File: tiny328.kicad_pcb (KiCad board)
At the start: 2 copper layers, 35.1 x 22.4 mm, 23 parts, among them IC1 ATMEGA328P-A, U1 RFM12, U2 MCP1702T-3302E/CB, Y1 16MHz

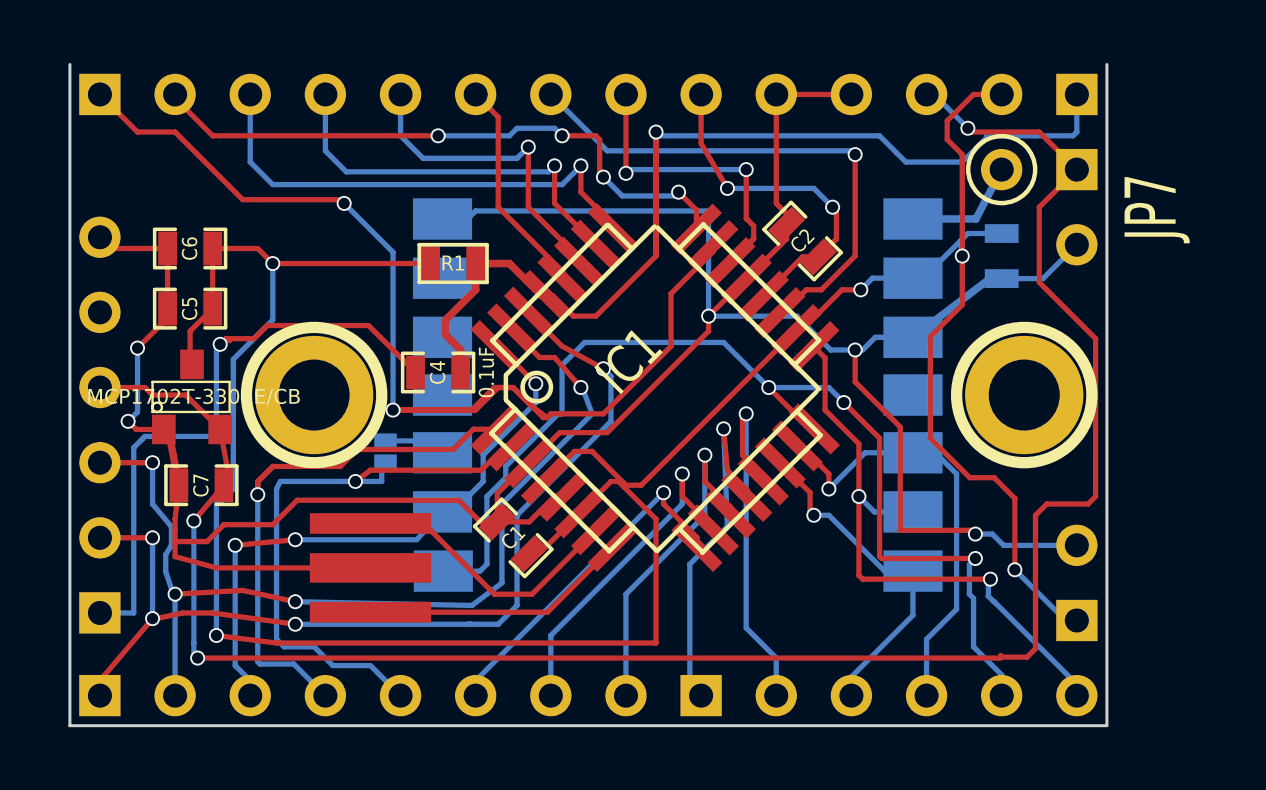
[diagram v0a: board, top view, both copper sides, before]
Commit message: increase power track widths
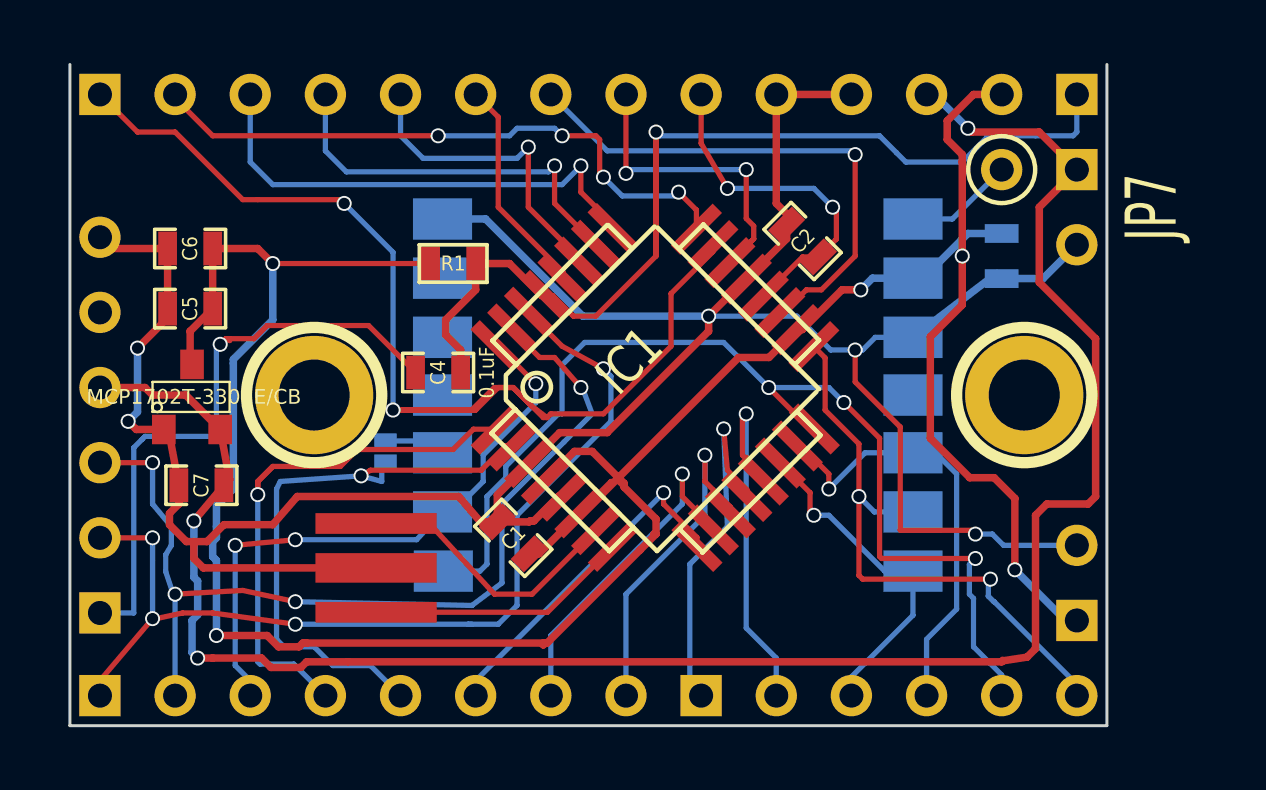
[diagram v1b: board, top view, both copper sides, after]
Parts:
- moved Y1 0.19 mm to (39.3, 31.0)
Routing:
- net GND: track 97.9 -> 95.2 mm

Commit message: widen vias
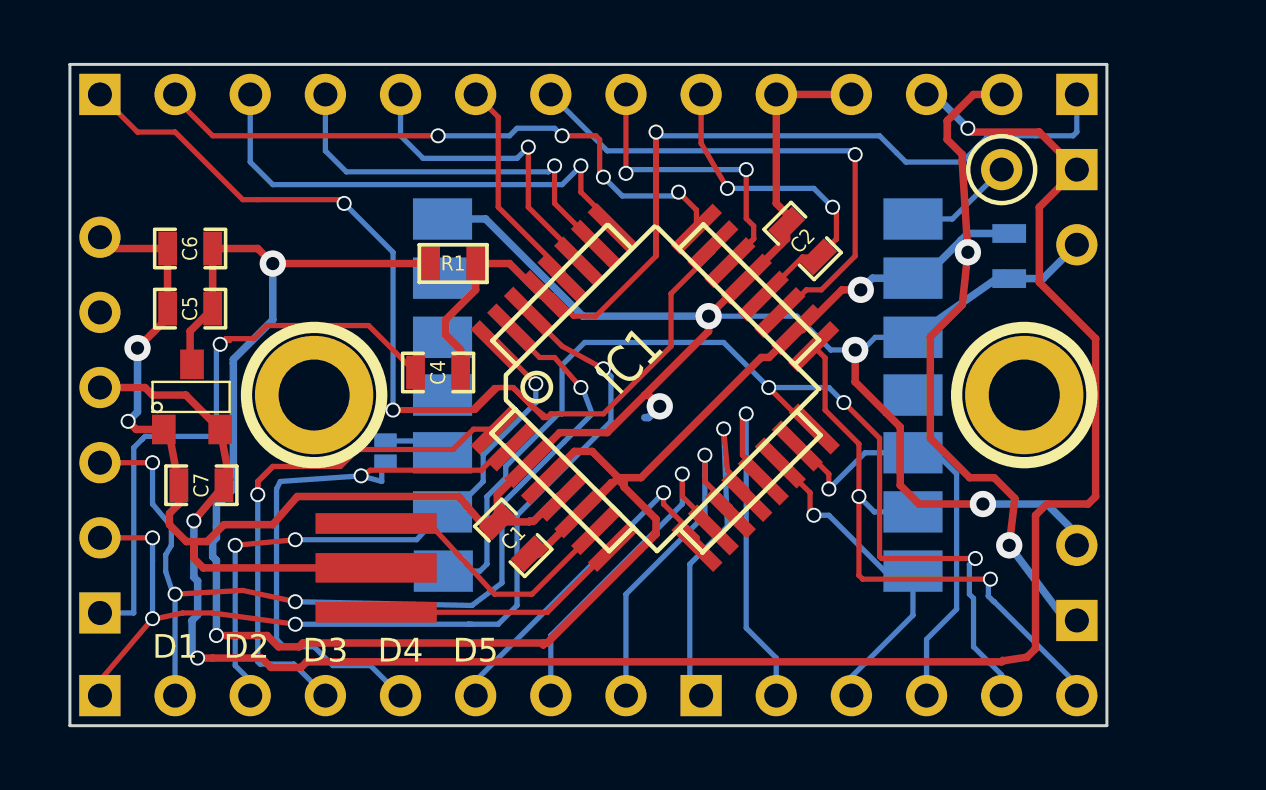
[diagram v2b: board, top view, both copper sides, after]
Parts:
- moved C3 0.25 mm to (60.7, 20.4)
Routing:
- net GND: track 95.2 -> 99.1 mm, vias 5 -> 6
- added copper zone on B.Cu, net GND
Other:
- board text added: "D1"
- board text added: "D2"
- board text added: "D3"
- board text added: "D4"
- board text added: "D5"

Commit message: all connected, flooded
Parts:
- moved C6 1.52 mm to (34.5, 20.2)
- moved C3 0.76 mm to (60.7, 21.2)
- moved C5 0.25 mm to (33.3, 22.2)
- moved C7 0.18 mm to (33.5, 28.1)
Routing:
- net GND: track 99.1 -> 102.9 mm
- net /D1/TX: track 32.8 -> 31.9 mm
- net 3V3: track 93.5 -> 94.2 mm
- net /D0/RX: track 33.1 -> 32.5 mm
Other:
- board text added: "3V3"
- board text added: "5"
- board text added: "5V"
- board text added: "6"
- board text added: "A"
- board text added: "A0"
- board text added: "A1"
- board text added: "A2"
- board text added: "A3"
- board text added: "A4"
- board text added: "A5"
- board text added: "A7"
- board text added: "ANT"
- board text added: "AREF"
- board text added: "D0 RX"
- board text added: "D1 TX"
- board text added: "D10"
- board text added: "D10*"
- board text added: "D11"
- board text added: "D11*"
- board text added: "D12"
- board text added: "D13"
- board text added: "D3*"
- board text added: "D3*I1"
- board text added: "D5*"
- board text added: "D6*"
- board text added: "D7"
- board text added: "D8"
- board text added: "D9"
- board text added: "D9*"
- board text added: "DTR"
- board text added: "GND"
- board text added: "I0"
- board text added: "I1"
- board text added: "MOSI"
- board text added: "RST"
- board text added: "RX"
- board text added: "RX D0"
- board text added: "SCL"
- board text added: "SDA"
- board text added: "SS"
- board text added: "TX"
- board text added: "TX D1"
- board text removed: "D1"
- board text removed: "D3"
- board text removed: "D5"

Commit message: all connected, flooded
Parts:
- added R2: 100K, SM0603, F.Cu at (33.4, 17.9)
- added R3: 100K, SM0603, F.Cu at (30.6, 17.8)

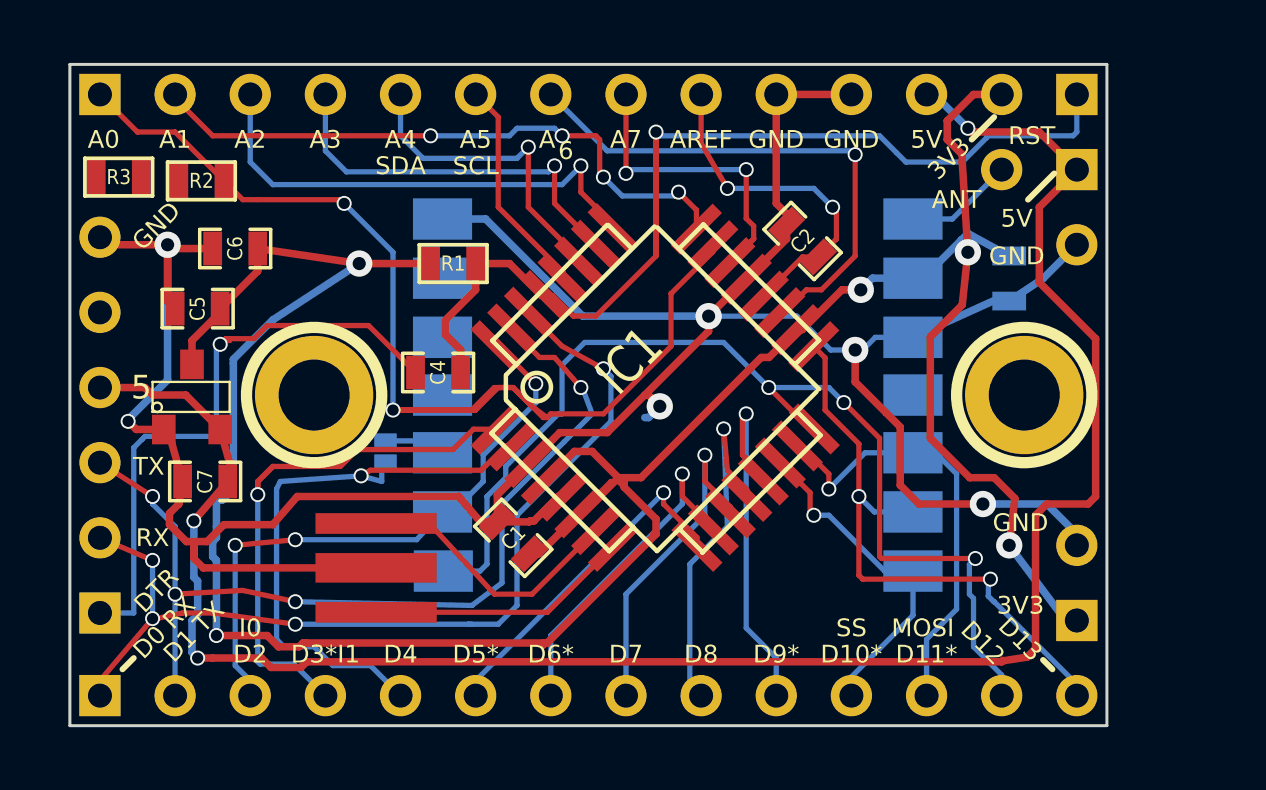
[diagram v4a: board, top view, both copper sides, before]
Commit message: first version sent to osh park
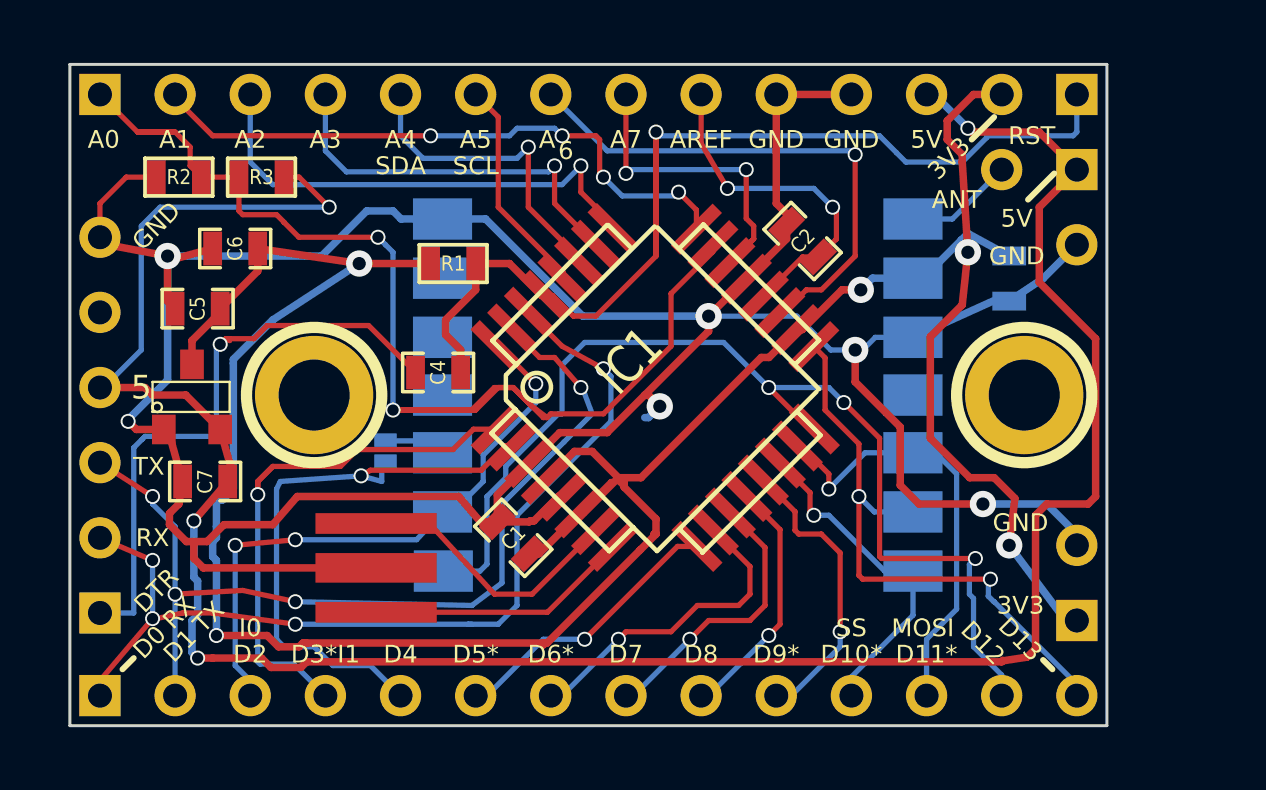
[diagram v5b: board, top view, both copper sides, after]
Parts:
- moved R3 4.83 mm to (35.4, 17.8), turned to 0 degrees
- moved R2 0.77 mm to (32.6, 17.8), turned to 180 degrees
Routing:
- net +5V: track 67.2 -> 81.9 mm, vias 3 -> 4
- net GND: track 102.9 -> 115.7 mm
- net /D8: track 12.3 -> 8.45 mm
- net /D9: track 12.5 -> 10.0 mm
- net /A0: track 42.2 -> 44.5 mm
- net /D5: track 11.8 -> 9.57 mm
- net /D7: track 11.5 -> 9.57 mm
- net /D6: track 11.7 -> 10.8 mm

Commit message: Increase header hole & pad size Fix MCP1800 reversed pins 2 & 3 Fix FTDI reversed TX & RX Add MISO & SCK labels Remove silk screen around mounting holes Increase pad size for 0603's for hand soldering
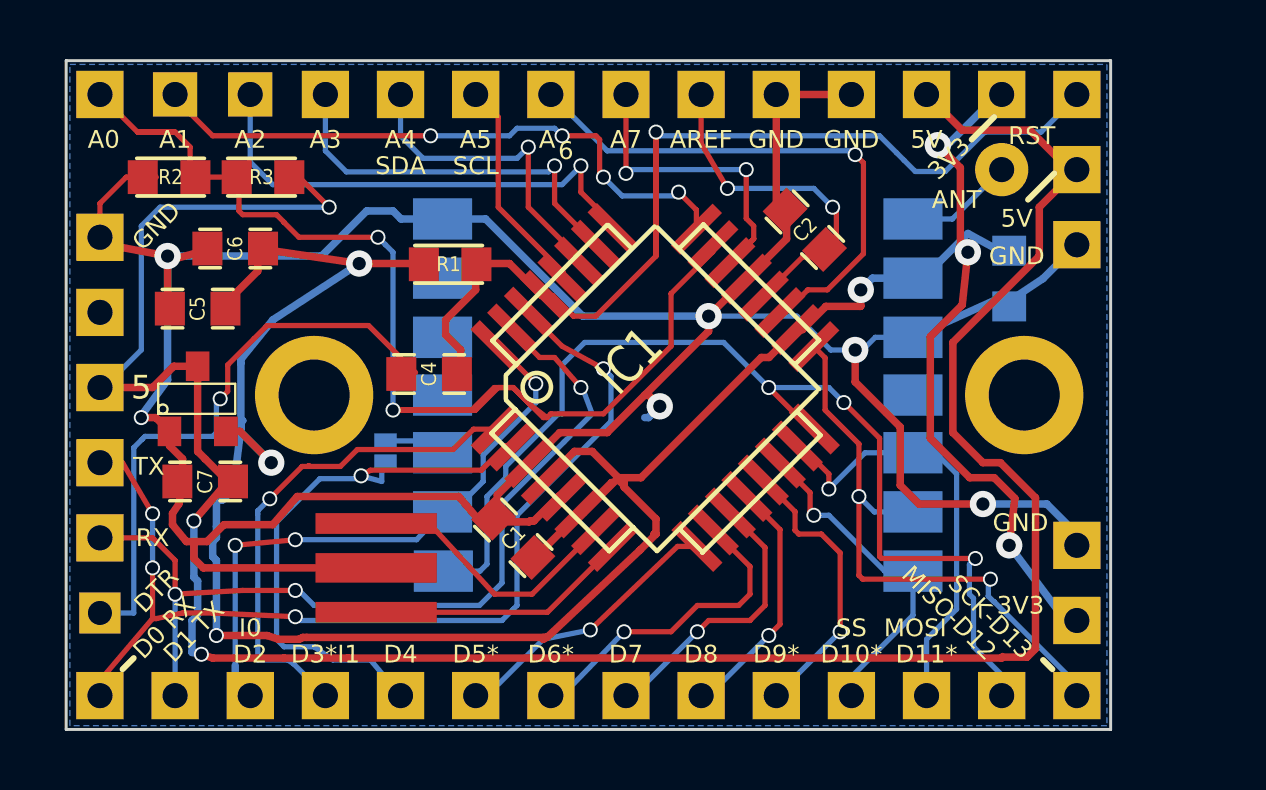
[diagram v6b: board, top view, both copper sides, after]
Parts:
- 1PIN (x2): footprint 1pin -> 1pin_only
- C1, C2, C3, C4, C5, C6, C7: footprint SM0603_Capa -> SM0603_C_Hand
- R1, R2, R3: footprint SM0603 -> SM0603_Hand
- U2: value MCP1702T-3302E/CB -> MCP1700
- moved C2 0.39 mm to (53.8, 19.6)
- moved C4 0.31 mm to (41.1, 24.4)
- moved R2 0.28 mm to (32.4, 17.8)
- moved U2 0.20 mm to (33.3, 25.3)
- moved R1 0.15 mm to (41.8, 20.7)
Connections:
- JP6 pad 2: /D0/RX -> /D1/TX
- JP6 pad 3: /D1/TX -> /D0/RX
- U2 pad 2: +5V -> 3V3
- U2 pad 3: 3V3 -> +5V
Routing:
- net /D0/RX: track 32.5 -> 34.8 mm
- net /D3: track 18.8 -> 17.1 mm
- net 3V3: track 94.2 -> 95.7 mm, vias 5 -> 7
- net /D1/TX: track 31.9 -> 30.4 mm, vias 4 -> 3
- net +5V: track 81.9 -> 83.2 mm, vias 4 -> 3
- net /D2: track 21.2 -> 20.4 mm
- net GND: track 115.7 -> 114.9 mm
- net N-0000017: track 20.4 -> 19.7 mm
- net /D4: track 20.0 -> 19.4 mm
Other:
- board size 35.1 x 22.4 mm -> 35.3 x 22.6 mm
- board text added: "MISO-D12"
- board text added: "SCK-D13"

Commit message: adjust silk screen to be visible when headers are mounted
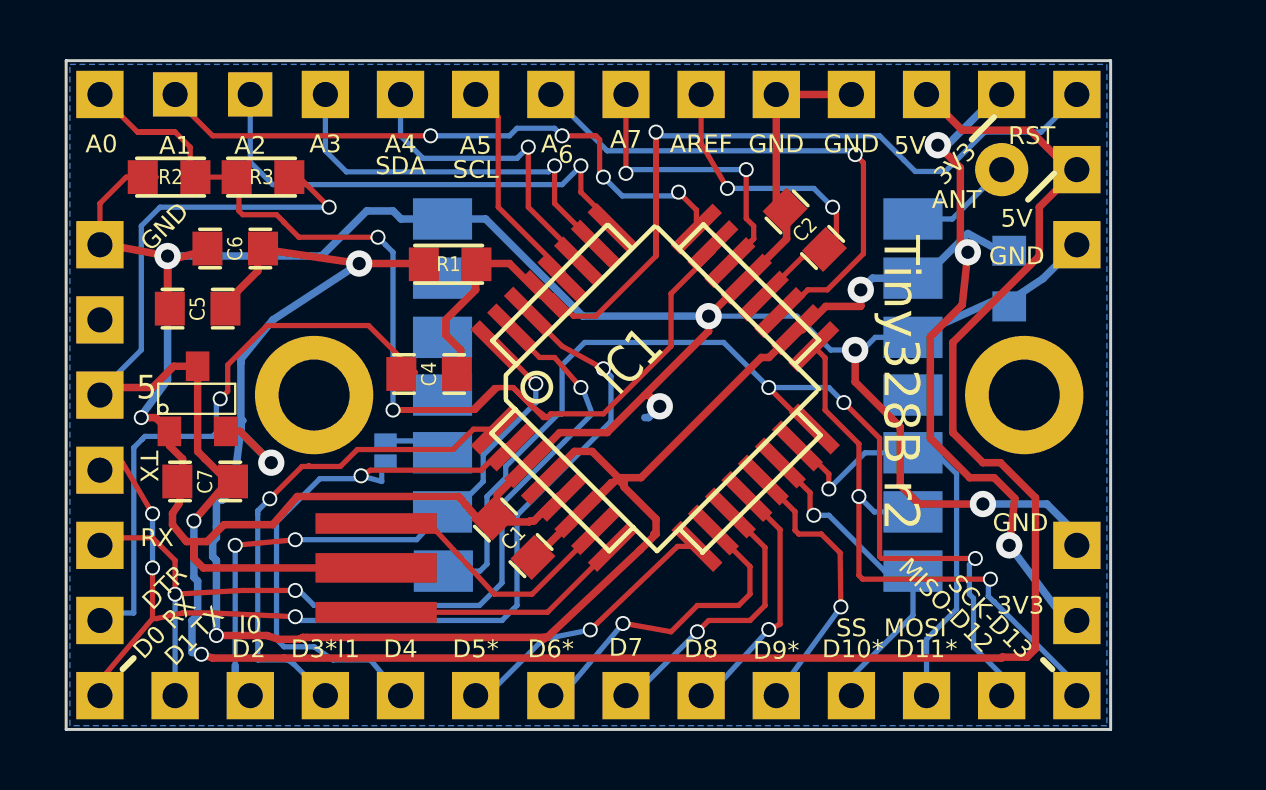
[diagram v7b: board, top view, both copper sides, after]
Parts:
- moved JP6 0.25 mm to (30.0, 26.4)
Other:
- board text added: "D1"
- board text added: "Tiny328B r2"
- board text removed: "D1 TX"
- board text removed: "D10"
- board text removed: "D11"
- board text removed: "D9"
